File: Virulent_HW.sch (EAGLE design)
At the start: 45 parts, among them U1 STM32F050G6U6

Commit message: Added the following components to library: SPST Switch, NFC Coil, Variable Capacitor. Updated circuitry to include NFC coil and tuning, initial state circuitry, and frequency modulation. Added appropriate data sheets.
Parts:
- added CT1: TZY2K450A001R002, Virulent_HW:TZY2K450A001R002
- added NFC1: WR-383250-17M2-G, Virulent_HW:WR-383250-17M2-G
- added R14, R15, R16, R17: NU, Virulent_HW:R-US_R0402
- added SPST1: FSA66SC70-5, Virulent_HW:FSA66SC70-5
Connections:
- removed net NFC_OUT: PLL1.INPUT@3, PLL2.INPUT@3, PLL3.INPUT@3
- new net MOD_FREQ: SPST1.OE@4
- new net N$25: R14.1, R15.2, U1IO.PA10@20
- new net N$26: CT1.A@1, NFC1.2@2
- new net N$28: R16.1, R17.2, U1IO.PA9@19
- new net NFC: NFC1.1@1, PLL1.INPUT@3, PLL2.INPUT@3, PLL3.INPUT@3, SPST1.B@2
- net +3.3V: now also R14.2, R16.2, SPST1.VCC@5
- net CARRIER_FREQ: now also SPST1.A@1
- net GND: now also CT1.B@2, R15.1, R17.1, SPST1.GND@3
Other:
- note added: "Frequency Modulation"
- note added: "Initial State Logic"
- note added: "NFC Transmitter"
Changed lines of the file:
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@@
 <part name="R13" library="Virulent_HW" deviceset="R-US_" device="R0402" value="10k"/>
 <part name="P+15" library="Virulent_HW" deviceset="+3.3V" device=""/>
+<part name="R14" library="Virulent_HW" deviceset="R-US_" device="R0402" value="NU"/>
+<part name="R15" library="Virulent_HW" deviceset="R-US_" device="R0402" value="NU"/>
+<part name="GND16" library="Virulent_HW" deviceset="GND" device=""/>
+<part name="P+16" library="Virulent_HW" deviceset="+3.3V" device=""/>
+<part name="R16" library="Virulent_HW" deviceset="R-US_" device="R0402" value="NU"/>
+<part name="R17" library="Virulent_HW" deviceset="R-US_" device="R0402" value="NU"/>
+<part name="GND17" library="Virulent_HW" deviceset="GND" device=""/>
+<part name="P+17" library="Virulent_HW" deviceset="+3.3V" device=""/>
+<part name="SPST1" library="Virulent_HW" deviceset="FSA66" device="SC70-5"/>
+<part name="P+18" library="Virulent_HW" deviceset="+3.3V" device=""/>
+<part name="GND18" library="Virulent_HW" deviceset="GND" device=""/>
+<part name="CT1" library="Virulent_HW" deviceset="TZY2K450A001R00" device="2"/>
+<part name="GND19" library="Virulent_HW" deviceset="GND" device=""/>
+<part name="NFC1" library="Virulent_HW" deviceset="WR-383250" device="-17M2-G"/>
 </parts>
 <sheets>
@@
 <text x="276.86" y="243.84" size="1.778" layer="97">STM32F050G6 Microcontroller</text>
 <wire x1="210.82" y1="246.38" x2="408.94" y2="246.38" width="0.1524" layer="97"/>
-<wire x1="408.94" y1="246.38" x2="408.94" y2="162.56" width="0.1524" layer="97"/>
-<wire x1="408.94" y1="162.56" x2="210.82" y2="162.56" width="0.1524" layer="97"/>
-<wire x1="210.82" y1="162.56" x2="210.82" y2="246.38" width="0.1524" layer="97"/>
+<wire x1="408.94" y1="246.38" x2="408.94" y2="157.48" width="0.1524" layer="97"/>
+<wire x1="408.94" y1="157.48" x2="210.82" y2="157.48" width="0.1524" layer="97"/>
+<wire x1="210.82" y1="157.48" x2="210.82" y2="246.38" width="0.1524" layer="97"/>
 <text x="50.8" y="71.12" size="1.778" layer="97">2kHz PLL</text>
 <text x="142.24" y="71.12" size="1.778" layer="97">3kHz PLL</text>
@@
 <wire x1="409.702" y1="96.52" x2="284.48" y2="96.52" width="0.1524" layer="97"/>
 <text x="340.36" y="93.98" size="1.778" layer="97">13.56 MHz Oscillator</text>
-<text x="297.18" y="167.64" size="1.778" layer="97">Pinout for IO is temporary</text>
+<text x="320.04" y="165.1" size="1.778" layer="97">Pinout for IO is temporary</text>
+<wire x1="284.48" y1="213.36" x2="314.96" y2="213.36" width="0.1524" layer="97" style="shortdash"/>
+<wire x1="314.96" y1="213.36" x2="314.96" y2="160.02" width="0.1524" layer="97" style="shortdash"/>
+<wire x1="314.96" y1="160.02" x2="284.48" y2="160.02" width="0.1524" layer="97" style="shortdash"/>
+<wire x1="284.48" y1="160.02" x2="284.48" y2="213.36" width="0.1524" layer="97" style="shortdash"/>
+<text x="292.1" y="210.82" size="1.778" layer="97">Initial State Logic</text>
+<wire x1="96.52" y1="114.3" x2="180.34" y2="114.3" width="0.1524" layer="97"/>
+<wire x1="180.34" y1="114.3" x2="180.34" y2="78.74" width="0.1524" layer="97"/>
+<wire x1="180.34" y1="78.74" x2="96.52" y2="78.74" width="0.1524" layer="97"/>
+<wire x1="96.52" y1="78.74" x2="96.52" y2="114.3" width="0.1524" layer="97"/>
+<text x="127" y="109.22" size="1.778" layer="97">Frequency Modulation</text>
+<wire x1="10.16" y1="114.3" x2="91.44" y2="114.3" width="0.1524" layer="97"/>
+<wire x1="91.44" y1="114.3" x2="91.44" y2="83.82" width="0.1524" layer="97"/>
+<wire x1="91.44" y1="83.82" x2="10.16" y2="83.82" width="0.1524" layer="97"/>
+<wire x1="10.16" y1="83.82" x2="10.16" y2="114.3" width="0.1524" layer="97"/>
+<text x="40.64" y="109.22" size="1.778" layer="97">NFC Transmitter</text>
 </plain>
 <instances>
@@
 <instance part="R13" gate="G$1" x="360.68" y="200.66" rot="R180"/>
 <instance part="P+15" gate="G$1" x="378.46" y="223.52"/>
+<instance part="R14" gate="G$1" x="304.8" y="182.88" rot="R90"/>
+<instance part="R15" gate="G$1" x="304.8" y="172.72" rot="R90"/>
+<instance part="GND16" gate="1" x="304.8" y="165.1"/>
+<instance part="P+16" gate="G$1" x="304.8" y="190.5"/>
+<instance part="R16" gate="G$1" x="292.1" y="200.66" rot="R90"/>
+<instance part="R17" gate="G$1" x="292.1" y="190.5" rot="R90"/>
+<instance part="GND17" gate="1" x="292.1" y="182.88"/>
+<instance part="P+17" gate="G$1" x="292.1" y="208.28"/>
+<instance part="SPST1" gate="G$1" x="139.7" y="93.98"/>
+<instance part="P+18" gate="G$1" x="157.48" y="101.6"/>
+<instance part="GND18" gate="1" x="127" y="83.82"/>
+<instance part="CT1" gate="G$1" x="66.04" y="96.52"/>
+<instance part="GND19" gate="1" x="71.12" y="91.44"/>
+<instance part="NFC1" gate="G$1" x="43.18" y="96.52"/>
 </instances>
 <busses>
@@
 <pinref part="RGB1" gate="G$1" pin="V+@4"/>
 <wire x1="378.46" y1="195.58" x2="383.54" y2="195.58" width="0.1524" layer="91"/>
+</segment>
+<segment>
+<pinref part="P+16" gate="G$1" pin="+3.3V"/>
+<pinref part="R14" gate="G$1" pin="2"/>
+</segment>
+<segment>
+<pinref part="P+17" gate="G$1" pin="+3.3V"/>
+<pinref part="R16" gate="G$1" pin="2"/>
+</segment>
+<segment>
+<pinref part="SPST1" gate="G$1" pin="VCC@5"/>
+<wire x1="149.86" y1="96.52" x2="157.48" y2="96.52" width="0.1524" layer="91"/>
+<pinref part="P+18" gate="G$1" pin="+3.3V"/>
+<wire x1="157.48" y1="96.52" x2="157.48" y2="99.06" width="0.1524" layer="91"/>
 </segment>
 </net>
@@
 <junction x="35.56" y="20.32"/>
 <junction x="83.82" y="20.32"/>
+<junction x="55.88" y="20.32"/>
 </segment>
 <segment>
@@
 <junction x="127" y="20.32"/>
 <junction x="175.26" y="20.32"/>
+<junction x="147.32" y="20.32"/>
 </segment>
 <segment>
@@
 <junction x="218.44" y="20.32"/>
 <junction x="266.7" y="20.32"/>
+<junction x="238.76" y="20.32"/>
 </segment>
 <segment>
@@
 <wire x1="264.16" y1="177.8" x2="264.16" y2="175.26" width="0.1524" layer="91"/>
 </segment>
+<segment>
+<pinref part="R15" gate="G$1" pin="1"/>
+<pinref part="GND16" gate="1" pin="GND"/>
+</segment>
+<segment>
+<pinref part="R17" gate="G$1" pin="1"/>
+<pinref part="GND17" gate="1" pin="GND"/>
+</segment>
+<segment>
+<pinref part="SPST1" gate="G$1" pin="GND@3"/>
+<wire x1="129.54" y1="88.9" x2="127" y2="88.9" width="0.1524" layer="91"/>
+<wire x1="127" y1="88.9" x2="127" y2="86.36" width="0.1524" layer="91"/>
+<pinref part="GND18" gate="1" pin="GND"/>
+</segment>
+<segment>
+<wire x1="68.58" y1="96.52" x2="69.85" y2="96.52" width="0.1524" layer="91"/>
+<wire x1="69.85" y1="96.52" x2="71.12" y2="96.52" width="0.1524" layer="91"/>
+<wire x1="71.12" y1="96.52" x2="71.12" y2="93.98" width="0.1524" layer="91"/>
+<pinref part="GND19" gate="1" pin="GND"/>
+<pinref part="CT1" gate="G$1" pin="B@2"/>
+<junction x="69.85" y="96.52"/>
+</segment>
 </net>
 <net name="5V_ENABLE" class="0">
@@
 </segment>
 </net>
-<net name="NFC_OUT" class="0">
+<net name="NFC" class="0">
 <segment>
 <pinref part="PLL1" gate="G$1" pin="INPUT@3"/>
@@
 <label x="218.44" y="43.18" size="1.778" layer="95" rot="R180" xref="yes"/>
 <wire x1="218.44" y1="43.18" x2="220.98" y2="43.18" width="0.1524" layer="91"/>
+</segment>
+<segment>
+<label x="27.94" y="96.52" size="1.778" layer="95" rot="R180" xref="yes"/>
+<wire x1="33.02" y1="96.52" x2="27.94" y2="96.52" width="0.1524" layer="91"/>
+<pinref part="NFC1" gate="G$1" pin="1@1"/>
+</segment>
+<segment>
+<pinref part="SPST1" gate="G$1" pin="B@2"/>
+<wire x1="129.54" y1="93.98" x2="121.92" y2="93.98" width="0.1524" layer="91"/>
+<label x="121.92" y="93.98" size="1.778" layer="95" rot="R180" xref="yes"/>
 </segment>
 </net>
@@
 <wire x1="370.84" y1="50.8" x2="358.14" y2="50.8" width="0.1524" layer="91"/>
 <junction x="370.84" y="68.58"/>
+<junction x="358.14" y="50.8"/>
 </segment>
 </net>
@@
 <wire x1="309.88" y1="66.04" x2="307.34" y2="66.04" width="0.1524" layer="91"/>
 <label x="307.34" y="66.04" size="1.778" layer="95" rot="R180" xref="yes"/>
+<junction x="309.88" y="66.04"/>
+<junction x="360.68" y="66.04"/>
+</segment>
+<segment>
+<pinref part="SPST1" gate="G$1" pin="A@1"/>
+<wire x1="129.54" y1="99.06" x2="121.92" y2="99.06" width="0.1524" layer="91"/>
+<label x="121.92" y="99.06" size="1.778" layer="95" rot="R180" xref="yes"/>
 </segment>
 </net>
@@
 <wire x1="314.96" y1="83.82" x2="314.96" y2="76.2" width="0.1524" layer="91"/>
 <junction x="314.96" y="76.2"/>
+<junction x="355.6" y="71.12"/>
 </segment>
 </net>
@@
 </segment>
 </net>
+<net name="N$25" class="0">
+<segment>
+<pinref part="U1" gate="IO" pin="PA10@20"/>
+<wire x1="317.5" y1="180.34" x2="312.42" y2="180.34" width="0.1524" layer="91"/>
+<wire x1="312.42" y1="180.34" x2="312.42" y2="177.8" width="0.1524" layer="91"/>
+<pinref part="R14" gate="G$1" pin="1"/>
+<pinref part="R15" gate="G$1" pin="2"/>
+<wire x1="312.42" y1="177.8" x2="304.8" y2="177.8" width="0.1524" layer="91"/>
+<junction x="304.8" y="177.8"/>
+</segment>
+</net>
+<net name="N$28" class="0">
+<segment>
+<pinref part="U1" gate="IO" pin="PA9@19"/>
+<wire x1="317.5" y1="185.42" x2="312.42" y2="185.42" width="0.1524" layer="91"/>
+<wire x1="312.42" y1="185.42" x2="312.42" y2="195.58" width="0.1524" layer="91"/>
+<pinref part="R16" gate="G$1" pin="1"/>
+<pinref part="R17" gate="G$1" pin="2"/>
+<wire x1="312.42" y1="195.58" x2="292.1" y2="195.58" width="0.1524" layer="91"/>
+<junction x="292.1" y="195.58"/>
+</segment>
+</net>
+<net name="MOD_FREQ" class="0">
+<segment>
+<pinref part="SPST1" gate="G$1" pin="OE@4"/>
+<wire x1="149.86" y1="91.44" x2="160.02" y2="91.44" width="0.1524" layer="91"/>
+<label x="160.02" y="91.44" size="1.778" layer="95" xref="yes"/>
+</segment>
+</net>
+<net name="N$26" class="0">
+<segment>
+<pinref part="NFC1" gate="G$1" pin="2@2"/>
+<pinref part="CT1" gate="G$1" pin="A@1"/>
+<wire x1="53.34" y1="96.52" x2="62.23" y2="96.52" width="0.1524" layer="91"/>
+</segment>
+</net>

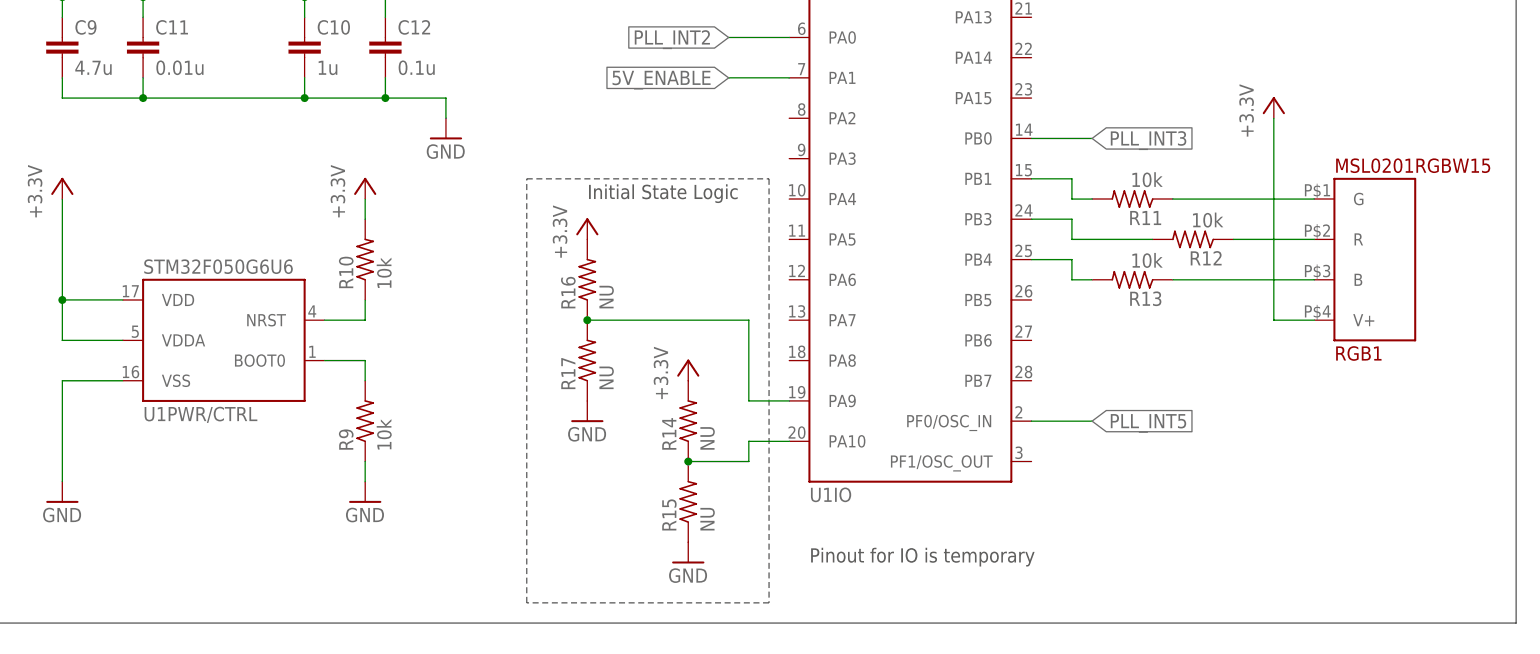
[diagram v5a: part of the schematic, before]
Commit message: updated LED symbol
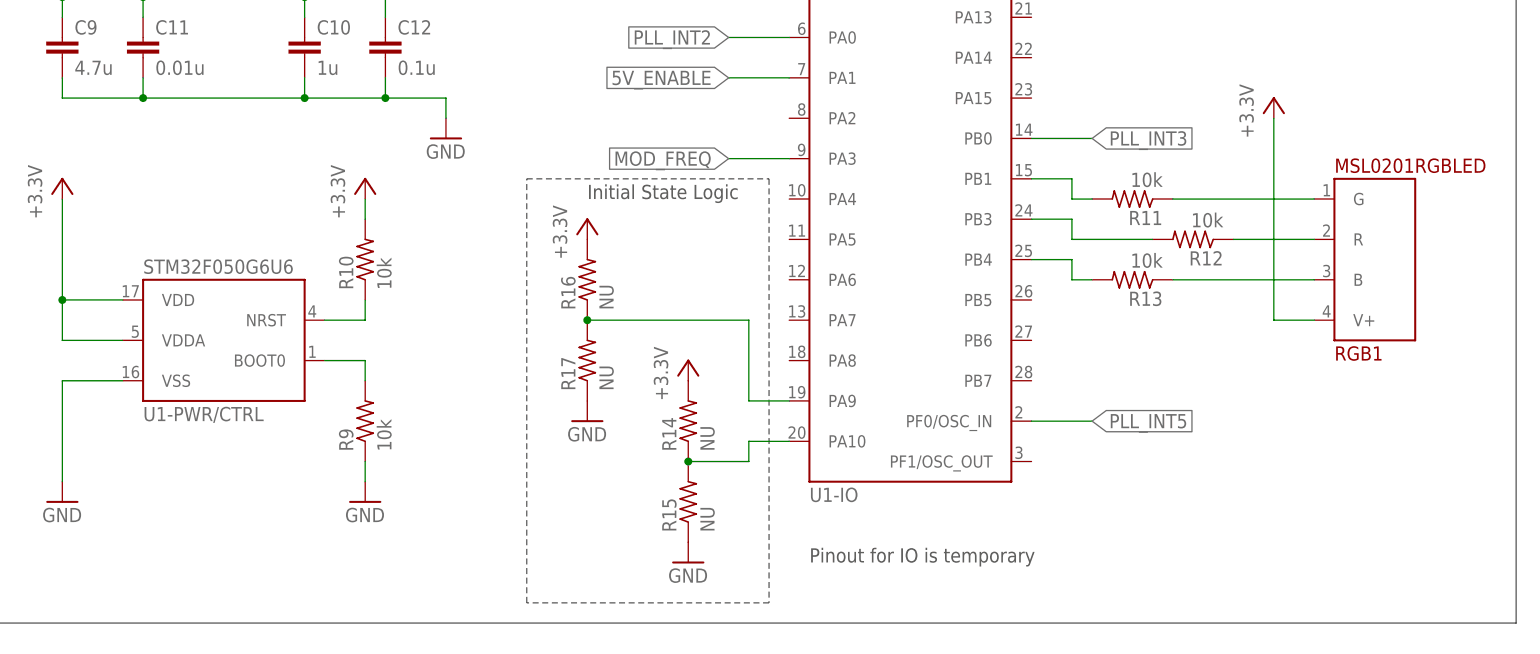
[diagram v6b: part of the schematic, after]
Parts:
- RGB1: value MSL0201RGBW15 -> MSL0201RGBLED; device Virulent_HW:MSL0201RGBW15 -> Virulent_HW:MSL0201RGBLED
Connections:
- net +3.3V: now also U1-PWR/CTRL.VDD@17, U1-PWR/CTRL.VDDA@5; no longer U1PWR/CTRL.VDD@17, U1PWR/CTRL.VDDA@5
- net 5V_ENABLE: now also U1-IO.PA1@7; no longer U1IO.PA1@7
- net GND: now also U1-PWR/CTRL.VSS@16; no longer U1PWR/CTRL.VSS@16
- net MOD_FREQ: now also U1-IO.PA3@9
- net N$21: now also U1-IO.PB1@15; no longer U1IO.PB1@15
- net N$22: now also U1-IO.PB3@24; no longer U1IO.PB3@24
- net N$23: now also U1-IO.PB4@25; no longer U1IO.PB4@25
- net N$25: now also U1-IO.PA10@20; no longer U1IO.PA10@20
- net N$28: now also U1-IO.PA9@19; no longer U1IO.PA9@19
- net N$6: now also U1-PWR/CTRL.NRST@4; no longer U1PWR/CTRL.NRST@4
- net N$9: now also U1-PWR/CTRL.BOOT0@1; no longer U1PWR/CTRL.BOOT0@1
- net PLL_INT2: now also U1-IO.PA0@6; no longer U1IO.PA0@6
- net PLL_INT3: now also U1-IO.PB0@14; no longer U1IO.PB0@14
- net PLL_INT5: now also U1-IO.PF0/OSC_IN@2; no longer U1IO.PF0/OSC_IN@2
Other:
- moved on the sheet: RGB1
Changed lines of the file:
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@@
 <part name="GND15" library="Virulent_HW" deviceset="GND" device=""/>
 <part name="P+14" library="Virulent_HW" deviceset="+3.3V" device=""/>
-<part name="RGB1" library="Virulent_HW" deviceset="MSL0201RGB" device="W15"/>
+<part name="RGB1" library="Virulent_HW" deviceset="MSL0201RGB" device="LED"/>
 <part name="R11" library="Virulent_HW" deviceset="R-US_" device="R0402" value="10k"/>
 <part name="R12" library="Virulent_HW" deviceset="R-US_" device="R0402" value="10k"/>
@@
 <instance part="P+9" gate="1" x="365.76" y="83.82"/>
 <instance part="GND13" gate="1" x="317.5" y="43.18"/>
-<instance part="U1" gate="PWR/CTRL" x="246.38" y="193.04"/>
-<instance part="U1" gate="IO" x="332.74" y="205.74"/>
+<instance part="U1" gate="-PWR/CTRL" x="246.38" y="193.04"/>
+<instance part="U1" gate="-IO" x="332.74" y="205.74"/>
 <instance part="P+10" gate="G$1" x="226.06" y="213.36"/>
 <instance part="GND14" gate="1" x="226.06" y="172.72"/>
@@
 </segment>
 <segment>
-<pinref part="U1" gate="PWR/CTRL" pin="VDDA@5"/>
+<pinref part="U1" gate="-PWR/CTRL" pin="VDDA@5"/>
 <pinref part="P+10" gate="G$1" pin="+3.3V"/>
 <wire x1="233.68" y1="193.04" x2="226.06" y2="193.04" width="0.1524" layer="91"/>
 <wire x1="226.06" y1="193.04" x2="226.06" y2="198.12" width="0.1524" layer="91"/>
-<pinref part="U1" gate="PWR/CTRL" pin="VDD@17"/>
+<pinref part="U1" gate="-PWR/CTRL" pin="VDD@17"/>
 <wire x1="226.06" y1="198.12" x2="226.06" y2="210.82" width="0.1524" layer="91"/>
 <wire x1="233.68" y1="198.12" x2="226.06" y2="198.12" width="0.1524" layer="91"/>
@@
 </segment>
 <segment>
-<pinref part="U1" gate="PWR/CTRL" pin="VSS@16"/>
+<pinref part="U1" gate="-PWR/CTRL" pin="VSS@16"/>
 <pinref part="GND14" gate="1" pin="GND"/>
 <wire x1="233.68" y1="187.96" x2="226.06" y2="187.96" width="0.1524" layer="91"/>
@@
 </segment>
 <segment>
-<pinref part="U1" gate="IO" pin="PA1@7"/>
+<pinref part="U1" gate="-IO" pin="PA1@7"/>
 <wire x1="317.5" y1="226.06" x2="309.88" y2="226.06" width="0.1524" layer="91"/>
 <label x="309.88" y="226.06" size="1.778" layer="97" rot="R180" xref="yes"/>
@@
 </segment>
 <segment>
-<pinref part="U1" gate="IO" pin="PA0@6"/>
+<pinref part="U1" gate="-IO" pin="PA0@6"/>
 <wire x1="317.5" y1="231.14" x2="309.88" y2="231.14" width="0.1524" layer="91"/>
 <label x="309.88" y="231.14" size="1.778" layer="97" rot="R180" xref="yes"/>
@@
 </segment>
 <segment>
-<pinref part="U1" gate="IO" pin="PB0@14"/>
+<pinref part="U1" gate="-IO" pin="PB0@14"/>
 <wire x1="347.98" y1="218.44" x2="355.6" y2="218.44" width="0.1524" layer="91"/>
 <label x="355.6" y="218.44" size="1.778" layer="97" xref="yes"/>
@@
 </segment>
 <segment>
-<pinref part="U1" gate="IO" pin="PF0/OSC_IN@2"/>
+<pinref part="U1" gate="-IO" pin="PF0/OSC_IN@2"/>
 <wire x1="347.98" y1="182.88" x2="355.6" y2="182.88" width="0.1524" layer="91"/>
 <label x="355.6" y="182.88" size="1.778" layer="97" xref="yes"/>
@@
 <net name="N$6" class="0">
 <segment>
-<pinref part="U1" gate="PWR/CTRL" pin="NRST@4"/>
+<pinref part="U1" gate="-PWR/CTRL" pin="NRST@4"/>
 <pinref part="R10" gate="G$1" pin="1"/>
 <wire x1="259.08" y1="195.58" x2="264.16" y2="195.58" width="0.1524" layer="91"/>
@@
 <net name="N$9" class="0">
 <segment>
-<pinref part="U1" gate="PWR/CTRL" pin="BOOT0@1"/>
+<pinref part="U1" gate="-PWR/CTRL" pin="BOOT0@1"/>
 <pinref part="R9" gate="G$1" pin="2"/>
 <wire x1="259.08" y1="190.5" x2="264.16" y2="190.5" width="0.1524" layer="91"/>
@@
 <pinref part="R11" gate="G$1" pin="2"/>
 <wire x1="355.6" y1="210.82" x2="353.06" y2="210.82" width="0.1524" layer="91"/>
-<pinref part="U1" gate="IO" pin="PB1@15"/>
+<pinref part="U1" gate="-IO" pin="PB1@15"/>
 <wire x1="353.06" y1="210.82" x2="353.06" y2="213.36" width="0.1524" layer="91"/>
 <wire x1="353.06" y1="213.36" x2="347.98" y2="213.36" width="0.1524" layer="91"/>
@@
 <wire x1="363.22" y1="205.74" x2="353.06" y2="205.74" width="0.1524" layer="91"/>
 <wire x1="353.06" y1="205.74" x2="353.06" y2="208.28" width="0.1524" layer="91"/>
-<pinref part="U1" gate="IO" pin="PB3@24"/>
+<pinref part="U1" gate="-IO" pin="PB3@24"/>
 <wire x1="353.06" y1="208.28" x2="347.98" y2="208.28" width="0.1524" layer="91"/>
 </segment>
@@
 <wire x1="355.6" y1="200.66" x2="353.06" y2="200.66" width="0.1524" layer="91"/>
 <wire x1="353.06" y1="200.66" x2="353.06" y2="203.2" width="0.1524" layer="91"/>
-<pinref part="U1" gate="IO" pin="PB4@25"/>
+<pinref part="U1" gate="-IO" pin="PB4@25"/>
 <wire x1="353.06" y1="203.2" x2="347.98" y2="203.2" width="0.1524" layer="91"/>
 </segment>
@@
 <net name="N$25" class="0">
 <segment>
-<pinref part="U1" gate="IO" pin="PA10@20"/>
+<pinref part="U1" gate="-IO" pin="PA10@20"/>
 <wire x1="317.5" y1="180.34" x2="312.42" y2="180.34" width="0.1524" layer="91"/>
 <wire x1="312.42" y1="180.34" x2="312.42" y2="177.8" width="0.1524" layer="91"/>
@@
 <net name="N$28" class="0">
 <segment>
-<pinref part="U1" gate="IO" pin="PA9@19"/>
+<pinref part="U1" gate="-IO" pin="PA9@19"/>
 <wire x1="317.5" y1="185.42" x2="312.42" y2="185.42" width="0.1524" layer="91"/>
 <wire x1="312.42" y1="185.42" x2="312.42" y2="195.58" width="0.1524" layer="91"/>
@@
 <label x="160.02" y="91.44" size="1.778" layer="95" xref="yes"/>
 </segment>
-</net>
+<segment>
+<pinref part="U1" gate="-IO" pin="PA3@9"/>
+<wire x1="317.5" y1="215.9" x2="309.88" y2="215.9" width="0.1524" layer="91"/>
+<label x="309.88" y="215.9" size="1.778" layer="95" rot="R180" xref="yes"/>
+</segment>
+</net>
